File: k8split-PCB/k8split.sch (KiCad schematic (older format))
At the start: 233 parts, among them J1 AVR-ISP-6, J13 Breakaway_Tabs, J14 Breakaway_Tabs, J17 Breakaway_Tabs, J18 Breakaway_Tabs, J19 Breakaway_Tabs, J2 AVR-ISP-6, J3 Breakaway_Tabs, J5 Breakaway_Tabs, J6 Breakaway_Tabs, J7 Breakaway_Tabs, J9 Breakaway_Tabs, SW1 SW_Push, SW2 SW_Push, U1 ATmega32U4-AU, U2 ATmega32U4-AU, Y1 16MHz, Y2 16MHz

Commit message: near completed routing on boards
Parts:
- added C6: 0.1uF, Capacitor_SMD:C_0603_1608Metric, symbol k8split-rescue:C_Small-Device-Orbit-rescue
- added H1, H2, H3, H4, H5, H6, H7, H8: MountingHole, MountingHole:MountingHole_3.2mm_M3, symbol Mechanical:MountingHole
- USB1, USB2: footprint CUI_UJ2-AH-4-SMT -> locallib:CUI_UJ2-AH-4-SMT
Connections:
- net +5V: now also C6.1
- net GND: now also C6.2
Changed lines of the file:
@@
 ROW4
 Wire Wire Line
-	1300 3675 2425 3675
+	1300 3675 1575 3675
 Wire Wire Line
-	1300 3875 2425 3875
+	1300 3875 1575 3875
 $Comp
 L k8split-rescue:C_Small-Device-Orbit-rescue C5
@@
 F 0 "USB2" H 3082 14467 50  0000 C CNN
 F 1 "USB_A_SMT" H 3082 14376 50  0000 C CNN
-F 2 "CUI_UJ2-AH-4-SMT" H 2975 14000 50  0001 L BNN
+F 2 "locallib:CUI_UJ2-AH-4-SMT" H 2975 14000 50  0001 L BNN
 F 3 "MANUFACTURER RECOMMENDATIONS" H 2975 14000 50  0001 L BNN
 F 4 "1.01" H 2975 14000 50  0001 L BNN "Field4"
@@
 F 0 "USB1" H 3107 6867 50  0000 C CNN
 F 1 "USB_A_SMT" H 3107 6776 50  0000 C CNN
-F 2 "CUI_UJ2-AH-4-SMT" H 3000 6400 50  0001 L BNN
+F 2 "locallib:CUI_UJ2-AH-4-SMT" H 3000 6400 50  0001 L BNN
 F 3 "MANUFACTURER RECOMMENDATIONS" H 3000 6400 50  0001 L BNN
 F 4 "1.01" H 3000 6400 50  0001 L BNN "Field4"
@@
 	3400 6500 3400 6700
 Connection ~ 3400 6700
+$Comp
+L k8split-rescue:C_Small-Device-Orbit-rescue C6
+U 1 1 5E1DFA40
+P 1575 3775
+F 0 "C6" H 1667 3821 50  0000 L CNN
+F 1 "0.1uF" H 1667 3730 50  0000 L CNN
+F 2 "Capacitor_SMD:C_0603_1608Metric" H 1575 3775 50  0001 C CNN
+F 3 "~" H 1575 3775 50  0001 C CNN
+	1    1575 3775
+	1    0    0    -1
+$EndComp
+Connection ~ 1575 3675
+Wire Wire Line
+	1575 3675 2425 3675
+Connection ~ 1575 3875
+Wire Wire Line
+	1575 3875 2425 3875
+$Comp
+L Mechanical:MountingHole H1
+U 1 1 5E3013F1
+P 6425 7375
+F 0 "H1" H 6525 7421 50  0000 L CNN
+F 1 "MountingHole" H 6525 7330 50  0000 L CNN
+F 2 "MountingHole:MountingHole_3.2mm_M3" H 6425 7375 50  0001 C CNN
+F 3 "~" H 6425 7375 50  0001 C CNN
+	1    6425 7375
+	1    0    0    -1
+$EndComp
+$Comp
+L Mechanical:MountingHole H2
+U 1 1 5E3013F7
+P 6425 7550
+F 0 "H2" H 6525 7596 50  0000 L CNN
+F 1 "MountingHole" H 6525 7505 50  0000 L CNN
+F 2 "MountingHole:MountingHole_3.2mm_M3" H 6425 7550 50  0001 C CNN
+F 3 "~" H 6425 7550 50  0001 C CNN
+	1    6425 7550
+	1    0    0    -1
+$EndComp
+$Comp
+L Mechanical:MountingHole H3
+U 1 1 5E3013FD
+P 7125 7375
+F 0 "H3" H 7225 7421 50  0000 L CNN
+F 1 "MountingHole" H 7225 7330 50  0000 L CNN
+F 2 "MountingHole:MountingHole_3.2mm_M3" H 7125 7375 50  0001 C CNN
+F 3 "~" H 7125 7375 50  0001 C CNN
+	1    7125 7375
+	1    0    0    -1
+$EndComp
+$Comp
+L Mechanical:MountingHole H4
+U 1 1 5E301403
+P 7125 7550
+F 0 "H4" H 7225 7596 50  0000 L CNN
+F 1 "MountingHole" H 7225 7505 50  0000 L CNN
+F 2 "MountingHole:MountingHole_3.2mm_M3" H 7125 7550 50  0001 C CNN
+F 3 "~" H 7125 7550 50  0001 C CNN
+	1    7125 7550
+	1    0    0    -1
+$EndComp
+$Comp
+L Mechanical:MountingHole H5
+U 1 1 5E329387
+P 6400 14975
+F 0 "H5" H 6500 15021 50  0000 L CNN
+F 1 "MountingHole" H 6500 14930 50  0000 L CNN
+F 2 "MountingHole:MountingHole_3.2mm_M3" H 6400 14975 50  0001 C CNN
+F 3 "~" H 6400 14975 50  0001 C CNN
+	1    6400 14975
+	1    0    0    -1
+$EndComp
+$Comp
+L Mechanical:MountingHole H6
+U 1 1 5E32938D
+P 6400 15150
+F 0 "H6" H 6500 15196 50  0000 L CNN
+F 1 "MountingHole" H 6500 15105 50  0000 L CNN
+F 2 "MountingHole:MountingHole_3.2mm_M3" H 6400 15150 50  0001 C CNN
+F 3 "~" H 6400 15150 50  0001 C CNN
+	1    6400 15150
+	1    0    0    -1
+$EndComp
+$Comp
+L Mechanical:MountingHole H7
+U 1 1 5E329393
+P 7100 14975
+F 0 "H7" H 7200 15021 50  0000 L CNN
+F 1 "MountingHole" H 7200 14930 50  0000 L CNN
+F 2 "MountingHole:MountingHole_3.2mm_M3" H 7100 14975 50  0001 C CNN
+F 3 "~" H 7100 14975 50  0001 C CNN
+	1    7100 14975
+	1    0    0    -1
+$EndComp
+$Comp
+L Mechanical:MountingHole H8
+U 1 1 5E329399
+P 7100 15150
+F 0 "H8" H 7200 15196 50  0000 L CNN
+F 1 "MountingHole" H 7200 15105 50  0000 L CNN
+F 2 "MountingHole:MountingHole_3.2mm_M3" H 7100 15150 50  0001 C CNN
+F 3 "~" H 7100 15150 50  0001 C CNN
+	1    7100 15150
+	1    0    0    -1
+$EndComp
 $EndSCHEMATC

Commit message: initial panelizing
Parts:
- removed J13, J14, J17, J18, J19: Breakaway_Tabs, locallib:breakaway-mousebites, symbol k8split-rescue:Conn_01x01-Connector_Generic-Orbit-rescue
- added J10, J4, J8: Breakaway_Tabs, locallib:breakaway-mousebites, symbol k8split-rescue:Conn_01x01-Connector_Generic-Orbit-rescue
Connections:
- no-connect marks 28 -> 26
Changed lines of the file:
@@
 Text Notes 5675 6500 0    50   ~ 0
 Extra Hardware
-$Comp
-L k8split-rescue:Conn_01x01-Connector_Generic-Orbit-rescue J3
-U 1 1 5BBDC449
-P 6000 6650
-F 0 "J3" H 6079 6692 50  0000 L CNN
-F 1 "Breakaway_Tabs" H 6079 6601 50  0000 L CNN
-F 2 "locallib:breakaway-mousebites" H 6000 6650 50  0001 C CNN
-F 3 "~" H 6000 6650 50  0001 C CNN
-	1    6000 6650
-	1    0    0    -1
-$EndComp
-NoConn ~ 5800 6650
-$Comp
-L k8split-rescue:Conn_01x01-Connector_Generic-Orbit-rescue J5
-U 1 1 5BBF47C0
-P 6000 7000
-F 0 "J5" H 6079 7042 50  0000 L CNN
-F 1 "Breakaway_Tabs" H 6079 6951 50  0000 L CNN
-F 2 "locallib:breakaway-mousebites" H 6000 7000 50  0001 C CNN
-F 3 "~" H 6000 7000 50  0001 C CNN
-	1    6000 7000
-	1    0    0    -1
-$EndComp
-NoConn ~ 5800 7000
-$Comp
-L k8split-rescue:Conn_01x01-Connector_Generic-Orbit-rescue J7
-U 1 1 5BC3C160
-P 6975 6650
-F 0 "J7" H 7054 6692 50  0000 L CNN
-F 1 "Breakaway_Tabs" H 7054 6601 50  0000 L CNN
-F 2 "locallib:breakaway-mousebites" H 6975 6650 50  0001 C CNN
-F 3 "~" H 6975 6650 50  0001 C CNN
-	1    6975 6650
-	1    0    0    -1
-$EndComp
-NoConn ~ 6775 6650
-$Comp
-L k8split-rescue:Conn_01x01-Connector_Generic-Orbit-rescue J9
-U 1 1 5BC3C16F
-P 6975 7000
-F 0 "J9" H 7054 7042 50  0000 L CNN
-F 1 "Breakaway_Tabs" H 7054 6951 50  0000 L CNN
-F 2 "locallib:breakaway-mousebites" H 6975 7000 50  0001 C CNN
-F 3 "~" H 6975 7000 50  0001 C CNN
-	1    6975 7000
-	1    0    0    -1
-$EndComp
-NoConn ~ 6775 7000
 Wire Notes Line
 	7750 11550 5650 11550
@@
 Text Notes 5675 14075 0    50   ~ 0
 Extra Hardware
-$Comp
-L k8split-rescue:Conn_01x01-Connector_Generic-Orbit-rescue J13
-U 1 1 5BCD1D3A
-P 6000 14225
-F 0 "J13" H 6079 14267 50  0000 L CNN
-F 1 "Breakaway_Tabs" H 6079 14176 50  0000 L CNN
-F 2 "locallib:breakaway-mousebites" H 6000 14225 50  0001 C CNN
-F 3 "~" H 6000 14225 50  0001 C CNN
-	1    6000 14225
-	1    0    0    -1
-$EndComp
-NoConn ~ 5800 14225
-$Comp
-L k8split-rescue:Conn_01x01-Connector_Generic-Orbit-rescue J17
-U 1 1 5BCD1D49
-P 6000 14575
-F 0 "J17" H 6079 14617 50  0000 L CNN
-F 1 "Breakaway_Tabs" H 6079 14526 50  0000 L CNN
-F 2 "locallib:breakaway-mousebites" H 6000 14575 50  0001 C CNN
-F 3 "~" H 6000 14575 50  0001 C CNN
-	1    6000 14575
-	1    0    0    -1
-$EndComp
-$Comp
-L k8split-rescue:Conn_01x01-Connector_Generic-Orbit-rescue J19
-U 1 1 5BCD1D50
-P 6000 14750
-F 0 "J19" H 6079 14792 50  0000 L CNN
-F 1 "Breakaway_Tabs" H 6079 14701 50  0000 L CNN
-F 2 "locallib:breakaway-mousebites" H 6000 14750 50  0001 C CNN
-F 3 "~" H 6000 14750 50  0001 C CNN
-	1    6000 14750
-	1    0    0    -1
-$EndComp
-NoConn ~ 5800 14750
-NoConn ~ 5800 14575
-$Comp
-L k8split-rescue:Conn_01x01-Connector_Generic-Orbit-rescue J14
-U 1 1 5BCD1D5A
-P 6975 14225
-F 0 "J14" H 7054 14267 50  0000 L CNN
-F 1 "Breakaway_Tabs" H 7054 14176 50  0000 L CNN
-F 2 "locallib:breakaway-mousebites" H 6975 14225 50  0001 C CNN
-F 3 "~" H 6975 14225 50  0001 C CNN
-	1    6975 14225
-	1    0    0    -1
-$EndComp
-NoConn ~ 6775 14225
-$Comp
-L k8split-rescue:Conn_01x01-Connector_Generic-Orbit-rescue J18
-U 1 1 5BCD1D69
-P 6975 14575
-F 0 "J18" H 7054 14617 50  0000 L CNN
-F 1 "Breakaway_Tabs" H 7054 14526 50  0000 L CNN
-F 2 "locallib:breakaway-mousebites" H 6975 14575 50  0001 C CNN
-F 3 "~" H 6975 14575 50  0001 C CNN
-	1    6975 14575
-	1    0    0    -1
-$EndComp
-NoConn ~ 6775 14575
 Text Notes 13050 7650 0    50   ~ 10
 LEFT HAND SCHEMATIC
@@
 Wire Notes Line
 	5650 675  5650 7700
-NoConn ~ 5800 7175
-$Comp
-L k8split-rescue:Conn_01x01-Connector_Generic-Orbit-rescue J6
-U 1 1 5BBF48DE
-P 6000 7175
-F 0 "J6" H 6079 7217 50  0000 L CNN
-F 1 "Breakaway_Tabs" H 6079 7126 50  0000 L CNN
-F 2 "locallib:breakaway-mousebites" H 6000 7175 50  0001 C CNN
-F 3 "~" H 6000 7175 50  0001 C CNN
-	1    6000 7175
-	1    0    0    -1
-$EndComp
 Connection ~ 1100 11550
 Connection ~ 1100 11350
@@
 	1575 3875 2425 3875
 $Comp
-L Mechanical:MountingHole H1
-U 1 1 5E3013F1
-P 6425 7375
-F 0 "H1" H 6525 7421 50  0000 L CNN
-F 1 "MountingHole" H 6525 7330 50  0000 L CNN
-F 2 "MountingHole:MountingHole_3.2mm_M3" H 6425 7375 50  0001 C CNN
-F 3 "~" H 6425 7375 50  0001 C CNN
-	1    6425 7375
-	1    0    0    -1
-$EndComp
-$Comp
 L Mechanical:MountingHole H2
 U 1 1 5E3013F7
@@
 	1    0    0    -1
 $EndComp
+$Comp
+L k8split-rescue:Conn_01x01-Connector_Generic-Orbit-rescue J3
+U 1 1 5E2DC692
+P 6075 6625
+F 0 "J3" H 6154 6667 50  0000 L CNN
+F 1 "Breakaway_Tabs" H 6154 6576 50  0000 L CNN
+F 2 "locallib:breakaway-mousebites" H 6075 6625 50  0001 C CNN
+F 3 "~" H 6075 6625 50  0001 C CNN
+	1    6075 6625
+	1    0    0    -1
+$EndComp
+NoConn ~ 5875 6625
+NoConn ~ 5875 6800
+$Comp
+L k8split-rescue:Conn_01x01-Connector_Generic-Orbit-rescue J6
+U 1 1 5E2DC6A0
+P 6075 7150
+F 0 "J6" H 6154 7192 50  0000 L CNN
+F 1 "Breakaway_Tabs" H 6154 7101 50  0000 L CNN
+F 2 "locallib:breakaway-mousebites" H 6075 7150 50  0001 C CNN
+F 3 "~" H 6075 7150 50  0001 C CNN
+	1    6075 7150
+	1    0    0    -1
+$EndComp
+NoConn ~ 5875 7150
+$Comp
+L k8split-rescue:Conn_01x01-Connector_Generic-Orbit-rescue J4
+U 1 1 5E2DC699
+P 6075 6800
+F 0 "J4" H 6154 6842 50  0000 L CNN
+F 1 "Breakaway_Tabs" H 6154 6751 50  0000 L CNN
+F 2 "locallib:breakaway-mousebites" H 6075 6800 50  0001 C CNN
+F 3 "~" H 6075 6800 50  0001 C CNN
+	1    6075 6800
+	1    0    0    -1
+$EndComp
+$Comp
+L k8split-rescue:Conn_01x01-Connector_Generic-Orbit-rescue J5
+U 1 1 5E2DC6AF
+P 6075 6975
+F 0 "J5" H 6154 7017 50  0000 L CNN
+F 1 "Breakaway_Tabs" H 6154 6926 50  0000 L CNN
+F 2 "locallib:breakaway-mousebites" H 6075 6975 50  0001 C CNN
+F 3 "~" H 6075 6975 50  0001 C CNN
+	1    6075 6975
+	1    0    0    -1
+$EndComp
+NoConn ~ 5875 6975
+$Comp
+L Mechanical:MountingHole H1
+U 1 1 5E3013F1
+P 6425 7375
+F 0 "H1" H 6525 7421 50  0000 L CNN
+F 1 "MountingHole" H 6525 7330 50  0000 L CNN
+F 2 "MountingHole:MountingHole_3.2mm_M3" H 6425 7375 50  0001 C CNN
+F 3 "~" H 6425 7375 50  0001 C CNN
+	1    6425 7375
+	1    0    0    -1
+$EndComp
+$Comp
+L k8split-rescue:Conn_01x01-Connector_Generic-Orbit-rescue J7
+U 1 1 5E3F5C7F
+P 6075 14175
+F 0 "J7" H 6154 14217 50  0000 L CNN
+F 1 "Breakaway_Tabs" H 6154 14126 50  0000 L CNN
+F 2 "locallib:breakaway-mousebites" H 6075 14175 50  0001 C CNN
+F 3 "~" H 6075 14175 50  0001 C CNN
+	1    6075 14175
+	1    0    0    -1
+$EndComp
+NoConn ~ 5875 14175
+NoConn ~ 5875 14350
+$Comp
+L k8split-rescue:Conn_01x01-Connector_Generic-Orbit-rescue J10
+U 1 1 5E3F5C87
+P 6075 14700
+F 0 "J10" H 6154 14742 50  0000 L CNN
+F 1 "Breakaway_Tabs" H 6154 14651 50  0000 L CNN
+F 2 "locallib:breakaway-mousebites" H 6075 14700 50  0001 C CNN
+F 3 "~" H 6075 14700 50  0001 C CNN
+	1    6075 14700
+	1    0    0    -1
+$EndComp
+NoConn ~ 5875 14700
+$Comp
+L k8split-rescue:Conn_01x01-Connector_Generic-Orbit-rescue J8
+U 1 1 5E3F5C8E
+P 6075 14350
+F 0 "J8" H 6154 14392 50  0000 L CNN
+F 1 "Breakaway_Tabs" H 6154 14301 50  0000 L CNN
+F 2 "locallib:breakaway-mousebites" H 6075 14350 50  0001 C CNN
+F 3 "~" H 6075 14350 50  0001 C CNN
+	1    6075 14350
+	1    0    0    -1
+$EndComp
+$Comp
+L k8split-rescue:Conn_01x01-Connector_Generic-Orbit-rescue J9
+U 1 1 5E3F5C94
+P 6075 14525
+F 0 "J9" H 6154 14567 50  0000 L CNN
+F 1 "Breakaway_Tabs" H 6154 14476 50  0000 L CNN
+F 2 "locallib:breakaway-mousebites" H 6075 14525 50  0001 C CNN
+F 3 "~" H 6075 14525 50  0001 C CNN
+	1    6075 14525
+	1    0    0    -1
+$EndComp
+NoConn ~ 5875 14525
 $EndSCHEMATC

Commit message: cleaned up libs and parts
- switched out 0805 resistors to 0603
- deleted some unused libraries
- re-associated symbols libs to point to system ones
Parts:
- C1, C10, C11, C14, C15, C16, C2, C3, C4, C5, C6, C7, C8, C9: symbol k8split-rescue:C_Small-Device-Orbit-rescue -> Device:C_Small
- D1, D10, D11, D12, D13, D14, D15, D16, D17, D18, D19, D2, D20, D21, D22, D23, D24, D25, D26, D27, D28, D29, D3, D30, D31, D32, D33, D34, D35, D36, D37, D38, D39, D4, D40, D41, D42, D43, D44, D45, D46, D47, D48, D49, D5, D50, D51, D52, D53, D54, D55, D56, D57, D58, D59, D6, D60, D61, D62, D63, D64, D65, D66, D67, D68, D69, D7, D70, D71, D72, D73, D74, D75, D76, D77, D78, D79, D8, D80, D81, D82, D83, D84, D85, D86, D87, D88, D89, D9, D90, D91, D92, D93, D94, D95, D96: symbol k8split-rescue:D_Small-Device-Orbit-rescue -> Device:D_Small
- J10, J3, J4, J5, J6, J7, J8, J9: symbol k8split-rescue:Conn_01x01-Connector_Generic-Orbit-rescue -> Connector_Generic:Conn_01x01
- R1, R2, R25, R3, R4, R5, R6, R67: footprint Resistor_SMD:R_0805_2012Metric -> Resistor_SMD:R_0603_1608Metric; symbol k8split-rescue:R_Small-Device-Orbit-rescue -> Device:R_Small
- SW1, SW2: symbol k8split-rescue:SW_Push-Switch-Orbit-rescue -> Switch:SW_Push
- Y1, Y2: symbol k8split-rescue:Crystal_GND24_Small-Device-Orbit-rescue -> Device:Crystal_GND24_Small
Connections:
- net +5V: no longer C4.1, C6.1
- net +5VA: no longer C11.1, C5.1
- net GND: no longer C2.2, C4.2, C6.2
- net GNDA: no longer C11.2, C5.2, C9.2
- net ROW0: no longer D1.1 (K), D13.1 (K), D19.1 (K), D25.1 (K), D31.1 (K), D37.1 (K), D7.1 (K)
- net ROW0-R: no longer D49.1 (K), D55.1 (K), D61.1 (K), D67.1 (K), D73.1 (K), D79.1 (K), D85.1 (K)
- net ROW1: no longer D14.1 (K), D2.1 (K), D20.1 (K), D26.1 (K), D32.1 (K), D38.1 (K), D8.1 (K)
- net ROW1-R: no longer D50.1 (K), D56.1 (K), D62.1 (K), D68.1 (K), D74.1 (K), D80.1 (K), D86.1 (K)
- net ROW2: no longer D15.1 (K), D21.1 (K), D27.1 (K), D3.1 (K), D33.1 (K), D39.1 (K), D9.1 (K)
- net ROW2-R: no longer D51.1 (K), D57.1 (K), D63.1 (K), D69.1 (K), D75.1 (K), D81.1 (K), D87.1 (K)
- net ROW3: no longer D10.1 (K), D16.1 (K), D22.1 (K), D28.1 (K), D34.1 (K), D4.1 (K), D40.1 (K)
- net ROW3-R: no longer D52.1 (K), D58.1 (K), D64.1 (K), D70.1 (K), D76.1 (K), D82.1 (K), D88.1 (K)
- net ROW4: no longer D11.1 (K), D17.1 (K), D23.1 (K), D29.1 (K), D35.1 (K), D41.1 (K), D5.1 (K)
- net ROW4-R: no longer D53.1 (K), D59.1 (K), D65.1 (K), D71.1 (K), D77.1 (K), D83.1 (K), D89.1 (K)
- net ROW5: no longer D12.1 (K), D18.1 (K), D24.1 (K), D30.1 (K), D36.1 (K), D42.1 (K), D6.1 (K)
- net ROW5-R: no longer D54.1 (K), D60.1 (K), D66.1 (K), D72.1 (K), D78.1 (K), D84.1 (K), D90.1 (K)
- net at C1.1, U1.17 (XTAL1): no longer Y1.1
- net at C2.1, U1.16 (XTAL2): no longer Y1.3
- net at C8.1, U2.17 (XTAL1): no longer Y2.1
- net at C9.1, U2.16 (XTAL2): no longer Y2.3

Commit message: further pcb project cleanup
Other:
- note added: "Credits to \nOrbit(x) by ai03 - Schematic and project fork base\nEverything else Orbit was based on\ntrifelife for mental support\nwhoever made that obscure smd usb model and footprint"
- note added: "RIGHT HAND SCHEMATIC"
- note removed: "Credits to \nOrbit(x) by ai03 - Schematic and project fork base\nEverything else Orbit was based on"
- note removed: "Passthrough Holes"
- note removed: "Passthrough Holes\n"
- note removed: "RIGHT HAND SCHEMATIC\n\nPower net changes:\nVCC -> VDD\nVBUS -> VDC\nGND -> GNDA\n+5V -> +5VA\nto prevent kicad from complaining about no connections between halves"
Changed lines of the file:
@@
 Text Notes 22250 15900 0    50   ~ 0
 0.1
-Text Notes 18700 15075 0    50   ~ 0
-Credits to \nOrbit(x) by ai03 - Schematic and project fork base\nEverything else Orbit was based on
+Text Notes 18700 15225 0    50   ~ 0
+Credits to \nOrbit(x) by ai03 - Schematic and project fork base\nEverything else Orbit was based on\ntrifelife for mental support\nwhoever made that obscure smd usb model and footprint
 Text Notes 5675 5350 0    50   ~ 0
 Indicator LEDs\n
@@
 Wire Notes Line
 	675  8250 13950 8250
-Wire Notes Line
-	675  12825 13950 12825
 Text Notes 7775 8350 0    50   ~ 0
 Switch Matrix\n
@@
 Wire Notes Line
 	13950 8250 13950 15275
-Text Notes 5675 12925 0    50   ~ 0
-Indicator LEDs\n
 Wire Notes Line
 	7750 8250 7750 15275
@@
 Text Notes 13050 7650 0    50   ~ 10
 LEFT HAND SCHEMATIC
-Text Notes 11100 15225 0    50   ~ 10
-RIGHT HAND SCHEMATIC\n\nPower net changes:\nVCC -> VDD\nVBUS -> VDC\nGND -> GNDA\n+5V -> +5VA\nto prevent kicad from complaining about no connections between halves
+Text Notes 13025 15250 0    50   ~ 10
+RIGHT HAND SCHEMATIC
 Wire Notes Line
 	9175 5250 9175 7700
 Wire Notes Line
 	5650 6400 9175 6400
-Wire Notes Line
-	9175 12825 9175 15275
-Wire Notes Line
-	5650 13975 9175 13975
-Text Notes 7775 12925 0    50   ~ 0
-Passthrough Holes\n
-Text Notes 7775 5350 0    50   ~ 0
-Passthrough Holes
 Text GLabel 9550 925  0    50   Input ~ 0
 COL0
@@
 Wire Wire Line
 	9150 12475 12375 12475
+Text Notes 5675 12925 0    50   ~ 0
+Indicator LEDs\n
+Wire Notes Line
+	675  12825 13950 12825
+Wire Notes Line
+	5650 13975 9175 13975
+Wire Notes Line
+	9175 12825 9175 15275
 $EndSCHEMATC

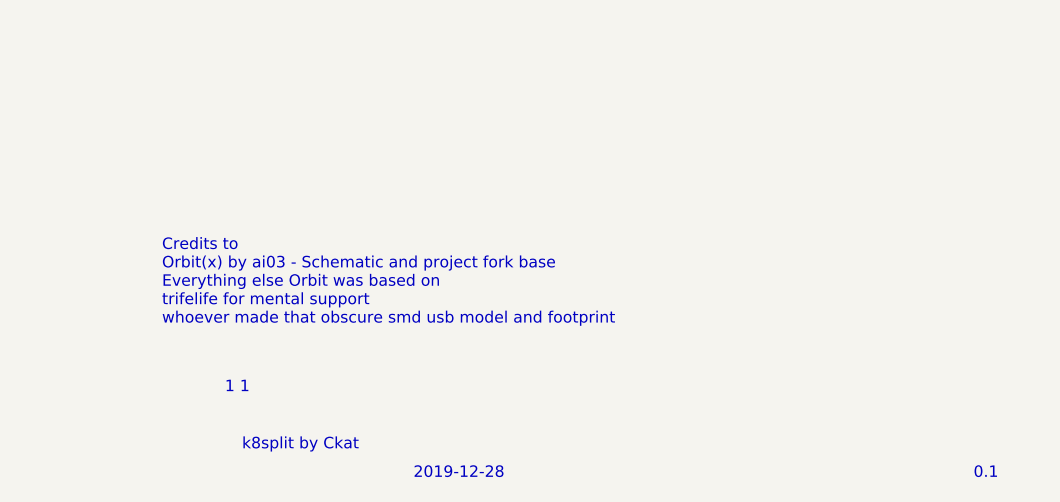
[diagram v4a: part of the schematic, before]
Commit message: update some minor schmetatic details
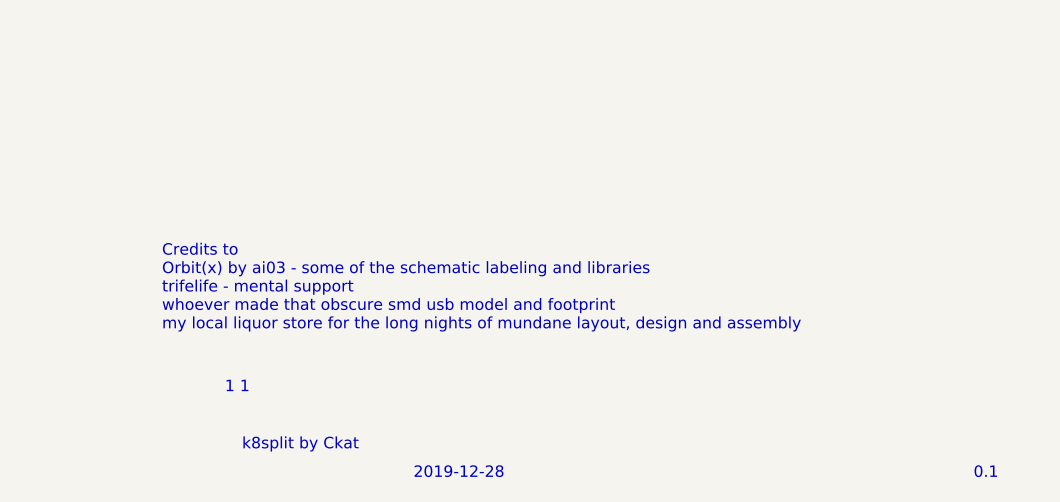
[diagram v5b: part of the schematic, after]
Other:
- note added: "Credits to \nOrbit(x) by ai03 - some of the schematic labeling and libraries\ntrifelife - mental support\nwhoever made that obscure smd usb model and footprint\nmy local liquor store for the long nights of mundane layout, design and assembly"
- note removed: "Credits to \nOrbit(x) by ai03 - Schematic and project fork base\nEverything else Orbit was based on\ntrifelife for mental support\nwhoever made that obscure smd usb model and footprint"
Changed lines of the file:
@@
 Text Notes 22250 15900 0    50   ~ 0
 0.1
-Text Notes 18700 15225 0    50   ~ 0
-Credits to \nOrbit(x) by ai03 - Schematic and project fork base\nEverything else Orbit was based on\ntrifelife for mental support\nwhoever made that obscure smd usb model and footprint
+Text Notes 18700 15250 0    50   ~ 0
+Credits to \nOrbit(x) by ai03 - some of the schematic labeling and libraries\ntrifelife - mental support\nwhoever made that obscure smd usb model and footprint\nmy local liquor store for the long nights of mundane layout, design and assembly
 Text Notes 5675 5350 0    50   ~ 0
 Indicator LEDs\n
